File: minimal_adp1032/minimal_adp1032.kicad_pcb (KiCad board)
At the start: 4 copper layers, 39.5 x 39.6 mm, 71 parts, among them J1 FW-02-03-G-D-085-155, J2 FW-02-03-G-D-085-155, J3 FW-07-03-G-D-085-155, J4 FW-07-03-G-D-085-155, J5 FW-02-03-G-D-085-155, J6 FW-02-03-G-D-085-155, T1 ZA9644-AED, U1 ADP1032ACPZ-5-R7

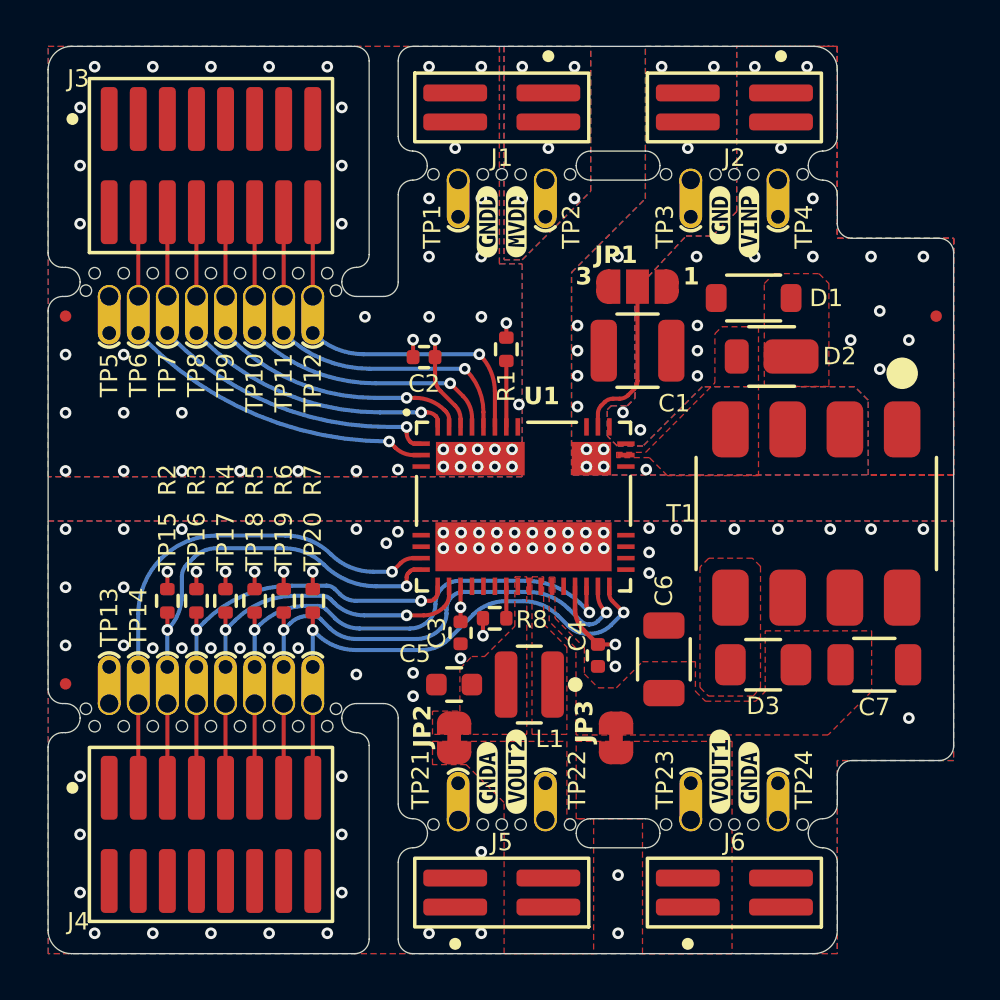
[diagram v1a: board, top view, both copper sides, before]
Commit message: Add new images and update project configuration for minimal_adp1032
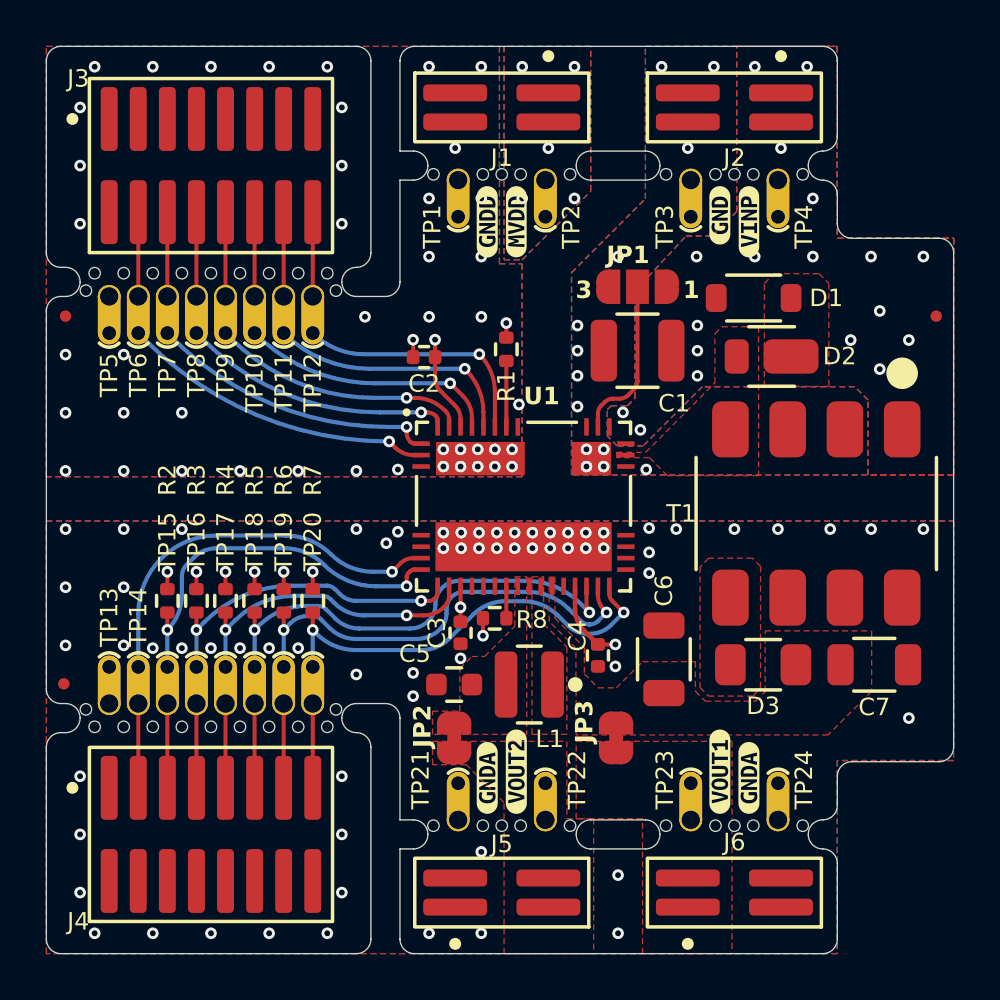
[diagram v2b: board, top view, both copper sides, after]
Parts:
- C2, C3, C4: value 0.1uF -> 100 nF
- C5: value 4.7 uF -> 4.7 µF
- C6, C7: value 10 uF -> 10 µF
- J3, J4: value FW-07-03-G-D-085-155 -> FW-08-03-G-D-085-155
- R1, R2, R3, R4, R5, R6, R7, R8: value 100k -> 100 kΩ
- moved FID2 0.08 mm to (132.6, 110.9)
- moved MB3 0.05 mm to (161.9, 117.5)
- moved MB4 0.05 mm to (151.8, 117.5)
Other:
- board size 39.5 x 39.6 mm -> 39.6 x 39.6 mm
